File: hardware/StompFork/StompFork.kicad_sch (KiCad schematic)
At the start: 32 parts, among them J1 Power, J2 Line-Level Input, J3 Direct Output, J4 Stompbox Output 1, J5 Stompbox Output 2, U1 TL074

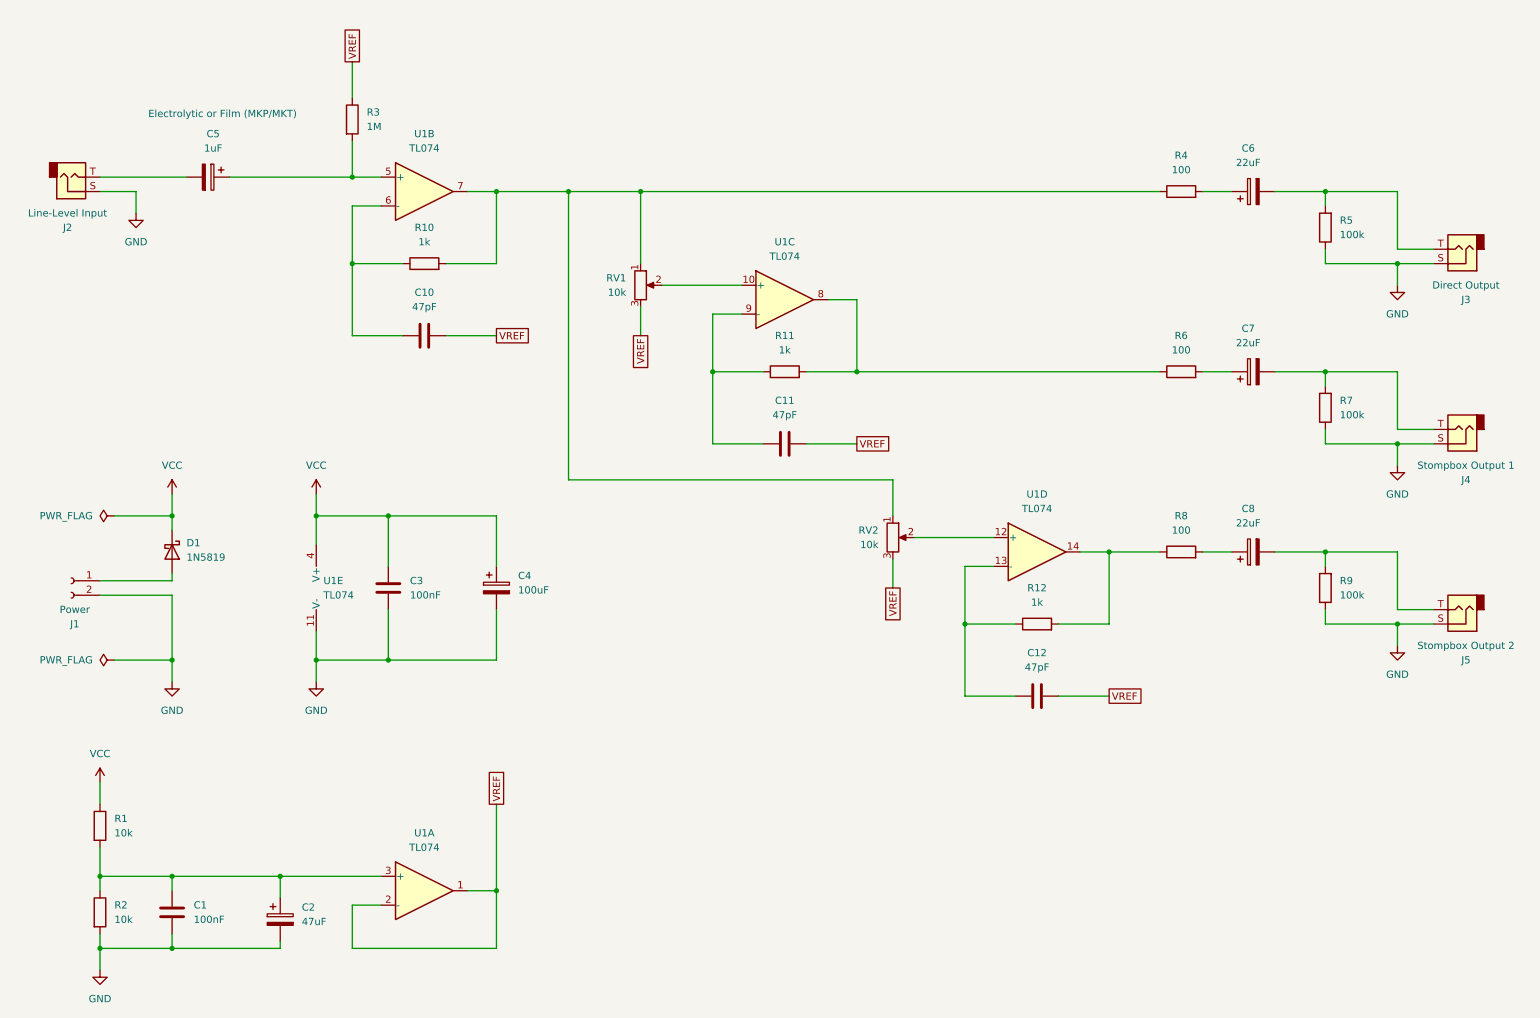
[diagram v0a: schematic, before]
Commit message: Fix part number order
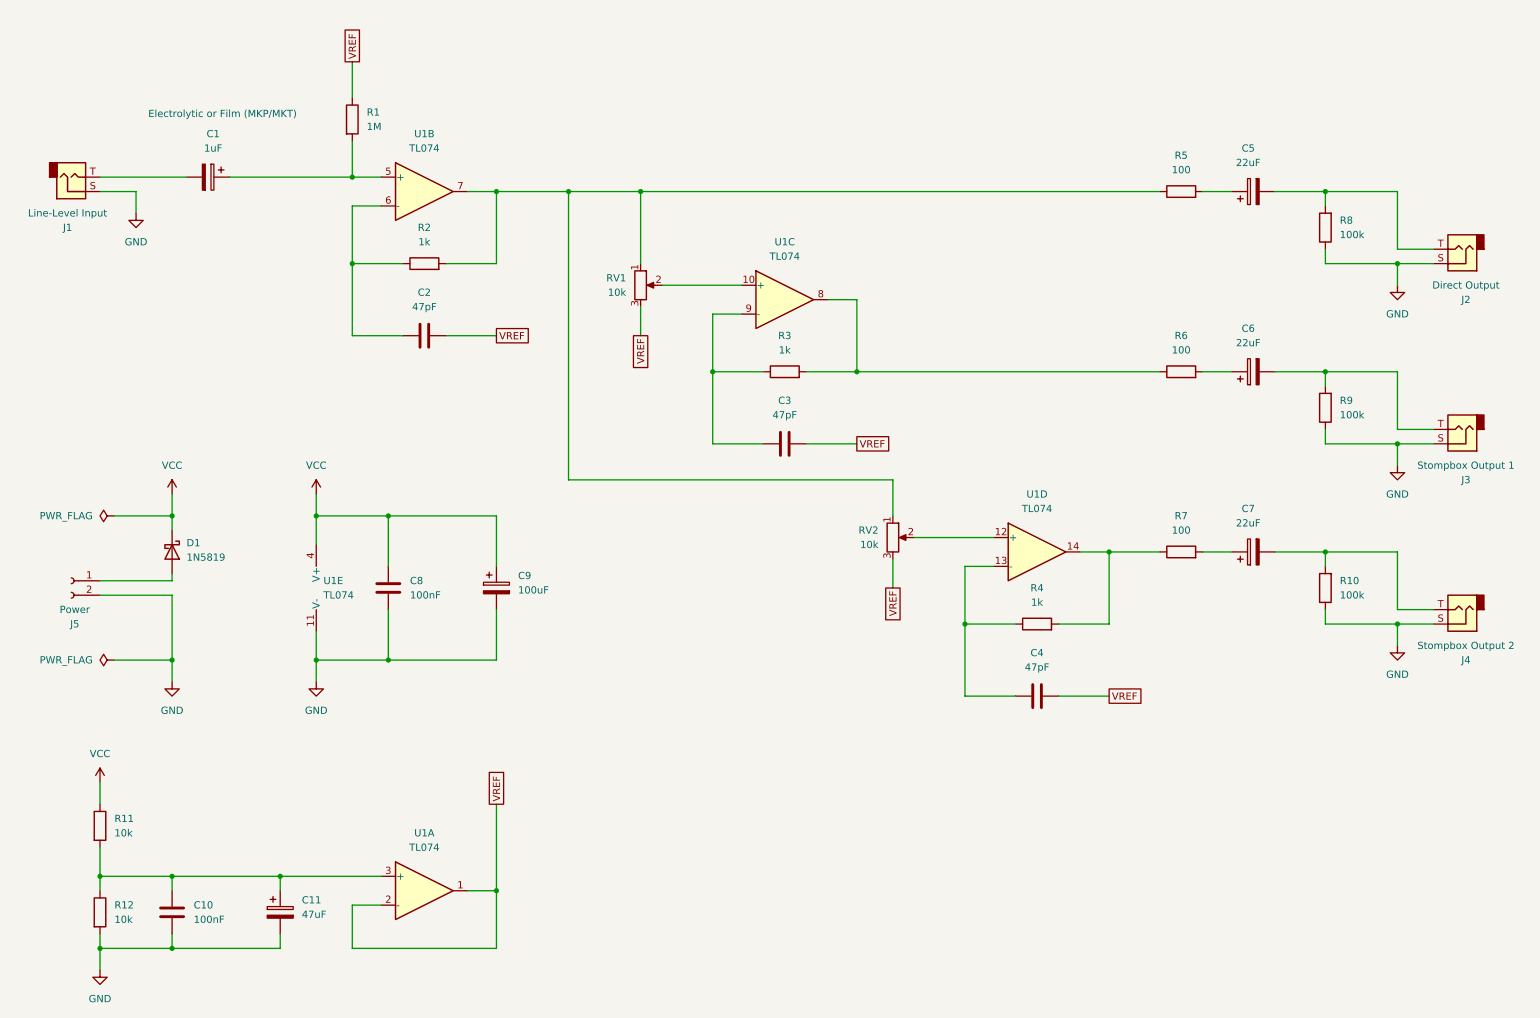
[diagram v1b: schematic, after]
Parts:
- renumbered C5 to C1, C1 to C10, C2 to C11, C10 to C2, C11 to C3, C12 to C4, C6 to C5, C7 to C6, C8 to C7, C3 to C8, C4 to C9, J2 to J1, J3 to J2, J4 to J3, J5 to J4, J1 to J5, R3 to R1, R9 to R10, R1 to R11, R2 to R12, R10 to R2, R11 to R3, R12 to R4, R4 to R5, R8 to R7, R5 to R8, R7 to R9
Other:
- title: (none) -> StompFork
- moved on the sheet: C11
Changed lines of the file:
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@@
 	(generator_version "9.0")
 	(paper "A4")
+	(title_block
+		(title "StompFork")
+		(date "2026")
+		(comment 1 "https://github.com/jurihock/StompFork")
+		(comment 3 "Active OpAmp audio signal splitter to feed multiple parallel stompboxes.")
+	)
 	(junction
 		(at 44.45 101.6)
@@
 	(wire
 		(pts
-			(xy 63.5 165.1) (xy 63.5 168.91)
+			(xy 63.5 165.1) (xy 63.5 167.64)
 		)
 		(stroke
@@
 	(wire
 		(pts
-			(xy 63.5 176.53) (xy 63.5 177.8)
+			(xy 63.5 175.26) (xy 63.5 177.8)
 		)
 		(stroke
@@
 		(on_board yes)
 		(dnp no)
-		(property "Reference" "R12"
+		(property "Reference" "R4"
 			(at 196.85 114.3 90)
 			(effects
@@
 			(project "StompFork"
 				(path "/9aeb4a2f-ec41-41a2-8cef-c6517b2f11ba"
-					(reference "R12")
+					(reference "R4")
 					(unit 1)
 				)
@@
 		(on_board yes)
 		(dnp no)
-		(property "Reference" "R10"
+		(property "Reference" "R2"
 			(at 88.9 50.8 90)
 			(effects
@@
 			(project "StompFork"
 				(path "/9aeb4a2f-ec41-41a2-8cef-c6517b2f11ba"
-					(reference "R10")
+					(reference "R2")
 					(unit 1)
 				)
@@
 		(dnp no)
 		(fields_autoplaced yes)
-		(property "Reference" "R3"
+		(property "Reference" "R1"
 			(at 78.74 30.4799 0)
 			(effects
@@
 			(project ""
 				(path "/9aeb4a2f-ec41-41a2-8cef-c6517b2f11ba"
-					(reference "R3")
+					(reference "R1")
 					(unit 1)
 				)
@@
 		(on_board yes)
 		(dnp no)
-		(property "Reference" "C5"
+		(property "Reference" "C1"
 			(at 51.689 34.29 90)
 			(effects
@@
 			(project ""
 				(path "/9aeb4a2f-ec41-41a2-8cef-c6517b2f11ba"
-					(reference "C5")
+					(reference "C1")
 					(unit 1)
 				)
@@
 		(on_board yes)
 		(dnp no)
-		(property "Reference" "R11"
+		(property "Reference" "R3"
 			(at 152.4 69.85 90)
 			(effects
@@
 			(project "StompFork"
 				(path "/9aeb4a2f-ec41-41a2-8cef-c6517b2f11ba"
-					(reference "R11")
+					(reference "R3")
 					(unit 1)
 				)
@@
 		(on_board yes)
 		(dnp no)
-		(property "Reference" "C12"
+		(property "Reference" "C4"
 			(at 196.85 125.73 90)
 			(effects
@@
 			(project "StompFork"
 				(path "/9aeb4a2f-ec41-41a2-8cef-c6517b2f11ba"
-					(reference "C12")
+					(reference "C4")
 					(unit 1)
 				)
@@
 		(dnp no)
 		(fields_autoplaced yes)
-		(property "Reference" "R4"
+		(property "Reference" "R5"
 			(at 222.25 38.1 90)
 			(effects
@@
 			(project ""
 				(path "/9aeb4a2f-ec41-41a2-8cef-c6517b2f11ba"
-					(reference "R4")
+					(reference "R5")
 					(unit 1)
 				)
@@
 		(on_board yes)
 		(dnp no)
-		(property "Reference" "J5"
+		(property "Reference" "J4"
 			(at 272.415 127 0)
 			(effects
@@
 			(project "StompFork"
 				(path "/9aeb4a2f-ec41-41a2-8cef-c6517b2f11ba"
-					(reference "J5")
+					(reference "J4")
 					(unit 1)
 				)
@@
 		(dnp no)
 		(fields_autoplaced yes)
-		(property "Reference" "C4"
+		(property "Reference" "C9"
 			(at 105.41 112.1409 0)
 			(effects
@@
 			(project "StompFork"
 				(path "/9aeb4a2f-ec41-41a2-8cef-c6517b2f11ba"
-					(reference "C4")
+					(reference "C9")
 					(unit 1)
 				)
@@
 	(symbol
 		(lib_id "Device:C_Polarized")
-		(at 63.5 172.72 0)
+		(at 63.5 171.45 0)
 		(unit 1)
 		(exclude_from_sim no)
@@
 		(dnp no)
 		(fields_autoplaced yes)
-		(property "Reference" "C2"
-			(at 67.31 170.5609 0)
+		(property "Reference" "C11"
+			(at 67.31 169.2909 0)
 			(effects
 				(font
@@
 		)
 		(property "Value" "47uF"
-			(at 67.31 173.1009 0)
+			(at 67.31 171.8309 0)
 			(effects
 				(font
@@
 		)
 		(property "Footprint" ""
-			(at 64.4652 176.53 0)
+			(at 64.4652 175.26 0)
 			(effects
 				(font
@@
 		)
 		(property "Datasheet" "~"
-			(at 63.5 172.72 0)
+			(at 63.5 171.45 0)
 			(effects
 				(font
@@
 		)
 		(property "Description" "Polarized capacitor"
-			(at 63.5 172.72 0)
+			(at 63.5 171.45 0)
 			(effects
 				(font
@@
 			(project "StompFork"
 				(path "/9aeb4a2f-ec41-41a2-8cef-c6517b2f11ba"
-					(reference "C2")
+					(reference "C11")
 					(unit 1)
 				)
@@
 		(on_board yes)
 		(dnp no)
-		(property "Reference" "J2"
+		(property "Reference" "J1"
 			(at 26.035 50.8 0)
 			(effects
@@
 			(project ""
 				(path "/9aeb4a2f-ec41-41a2-8cef-c6517b2f11ba"
-					(reference "J2")
+					(reference "J1")
 					(unit 1)
 				)
@@
 		(dnp no)
 		(fields_autoplaced yes)
-		(property "Reference" "C1"
+		(property "Reference" "C10"
 			(at 48.26 170.1799 0)
 			(effects
@@
 			(project "StompFork"
 				(path "/9aeb4a2f-ec41-41a2-8cef-c6517b2f11ba"
-					(reference "C1")
+					(reference "C10")
 					(unit 1)
 				)
@@
 		(dnp no)
 		(fields_autoplaced yes)
-		(property "Reference" "C8"
+		(property "Reference" "C7"
 			(at 234.061 100.33 90)
 			(effects
@@
 			(project "StompFork"
 				(path "/9aeb4a2f-ec41-41a2-8cef-c6517b2f11ba"
-					(reference "C8")
+					(reference "C7")
 					(unit 1)
 				)
@@
 		(dnp no)
 		(fields_autoplaced yes)
-		(property "Reference" "R8"
+		(property "Reference" "R7"
 			(at 222.25 101.6 90)
 			(effects
@@
 			(project "StompFork"
 				(path "/9aeb4a2f-ec41-41a2-8cef-c6517b2f11ba"
-					(reference "R8")
+					(reference "R7")
 					(unit 1)
 				)
@@
 		(dnp no)
 		(fields_autoplaced yes)
-		(property "Reference" "R7"
+		(property "Reference" "R9"
 			(at 250.19 81.2799 0)
 			(effects
@@
 			(project "StompFork"
 				(path "/9aeb4a2f-ec41-41a2-8cef-c6517b2f11ba"
-					(reference "R7")
+					(reference "R9")
 					(unit 1)
 				)
@@
 		(dnp no)
 		(fields_autoplaced yes)
-		(property "Reference" "C3"
+		(property "Reference" "C8"
 			(at 86.36 113.0299 0)
 			(effects
@@
 			(project "StompFork"
 				(path "/9aeb4a2f-ec41-41a2-8cef-c6517b2f11ba"
-					(reference "C3")
+					(reference "C8")
 					(unit 1)
 				)
@@
 		(dnp no)
 		(fields_autoplaced yes)
-		(property "Reference" "R9"
+		(property "Reference" "R10"
 			(at 250.19 113.0299 0)
 			(effects
@@
 			(project "StompFork"
 				(path "/9aeb4a2f-ec41-41a2-8cef-c6517b2f11ba"
-					(reference "R9")
+					(reference "R10")
 					(unit 1)
 				)
@@
 		(on_board yes)
 		(dnp no)
-		(property "Reference" "J4"
+		(property "Reference" "J3"
 			(at 272.415 95.25 0)
 			(effects
@@
 			(project "StompFork"
 				(path "/9aeb4a2f-ec41-41a2-8cef-c6517b2f11ba"
-					(reference "J4")
+					(reference "J3")
 					(unit 1)
 				)
@@
 		(dnp no)
 		(fields_autoplaced yes)
-		(property "Reference" "R1"
+		(property "Reference" "R11"
 			(at 34.29 154.9399 0)
 			(effects
@@
 			(project ""
 				(path "/9aeb4a2f-ec41-41a2-8cef-c6517b2f11ba"
-					(reference "R1")
+					(reference "R11")
 					(unit 1)
 				)
@@
 		(dnp no)
 		(fields_autoplaced yes)
-		(property "Reference" "C6"
+		(property "Reference" "C5"
 			(at 234.061 36.83 90)
 			(effects
@@
 			(project ""
 				(path "/9aeb4a2f-ec41-41a2-8cef-c6517b2f11ba"
-					(reference "C6")
+					(reference "C5")
 					(unit 1)
 				)
@@
 		(on_board yes)
 		(dnp no)
-		(property "Reference" "J3"
+		(property "Reference" "J2"
 			(at 272.415 63.5 0)
 			(effects
@@
 			(project "StompFork"
 				(path "/9aeb4a2f-ec41-41a2-8cef-c6517b2f11ba"
-					(reference "J3")
+					(reference "J2")
 					(unit 1)
 				)
@@
 		(on_board yes)
 		(dnp no)
-		(property "Reference" "C11"
+		(property "Reference" "C3"
 			(at 152.4 81.28 90)
 			(effects
@@
 			(project "StompFork"
 				(path "/9aeb4a2f-ec41-41a2-8cef-c6517b2f11ba"
-					(reference "C11")
+					(reference "C3")
 					(unit 1)
 				)
@@
 		(on_board yes)
 		(dnp no)
-		(property "Reference" "J1"
+		(property "Reference" "J5"
 			(at 27.305 120.65 0)
 			(effects
@@
 			(project ""
 				(path "/9aeb4a2f-ec41-41a2-8cef-c6517b2f11ba"
-					(reference "J1")
+					(reference "J5")
 					(unit 1)
 				)
@@
 		(dnp no)
 		(fields_autoplaced yes)
-		(property "Reference" "C7"
+		(property "Reference" "C6"
 			(at 234.061 68.58 90)
 			(effects
@@
 			(project "StompFork"
 				(path "/9aeb4a2f-ec41-41a2-8cef-c6517b2f11ba"
-					(reference "C7")
+					(reference "C6")
 					(unit 1)
 				)
@@
 		(on_board yes)
 		(dnp no)
-		(property "Reference" "C10"
+		(property "Reference" "C2"
 			(at 88.9 62.23 90)
 			(effects
@@
 			(project "StompFork"
 				(path "/9aeb4a2f-ec41-41a2-8cef-c6517b2f11ba"
-					(reference "C10")
+					(reference "C2")
 					(unit 1)
 				)
@@
 		(dnp no)
 		(fields_autoplaced yes)
-		(property "Reference" "R2"
+		(property "Reference" "R12"
 			(at 34.29 170.1799 0)
 			(effects
@@
 			(project "StompFork"
 				(path "/9aeb4a2f-ec41-41a2-8cef-c6517b2f11ba"
-					(reference "R2")
+					(reference "R12")
 					(unit 1)
 				)
@@
 		(dnp no)
 		(fields_autoplaced yes)
-		(property "Reference" "R5"
+		(property "Reference" "R8"
 			(at 250.19 49.5299 0)
 			(effects
@@
 			(project "StompFork"
 				(path "/9aeb4a2f-ec41-41a2-8cef-c6517b2f11ba"
-					(reference "R5")
+					(reference "R8")
 					(unit 1)
 				)
